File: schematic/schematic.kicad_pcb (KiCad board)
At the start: 2 copper layers, 18 parts, among them U2 74HC595

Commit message: Add outline to pcb
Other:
- board outline added: 66 x 46 mm
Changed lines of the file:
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@@
 		)
+	)
+	(gr_rect
+		(start 92 74.5)
+		(end 158 120.5)
+		(stroke
+			(width 0.1)
+			(type default)
+		)
+		(fill no)
+		(layer "Edge.Cuts")
 	)
 	(segment

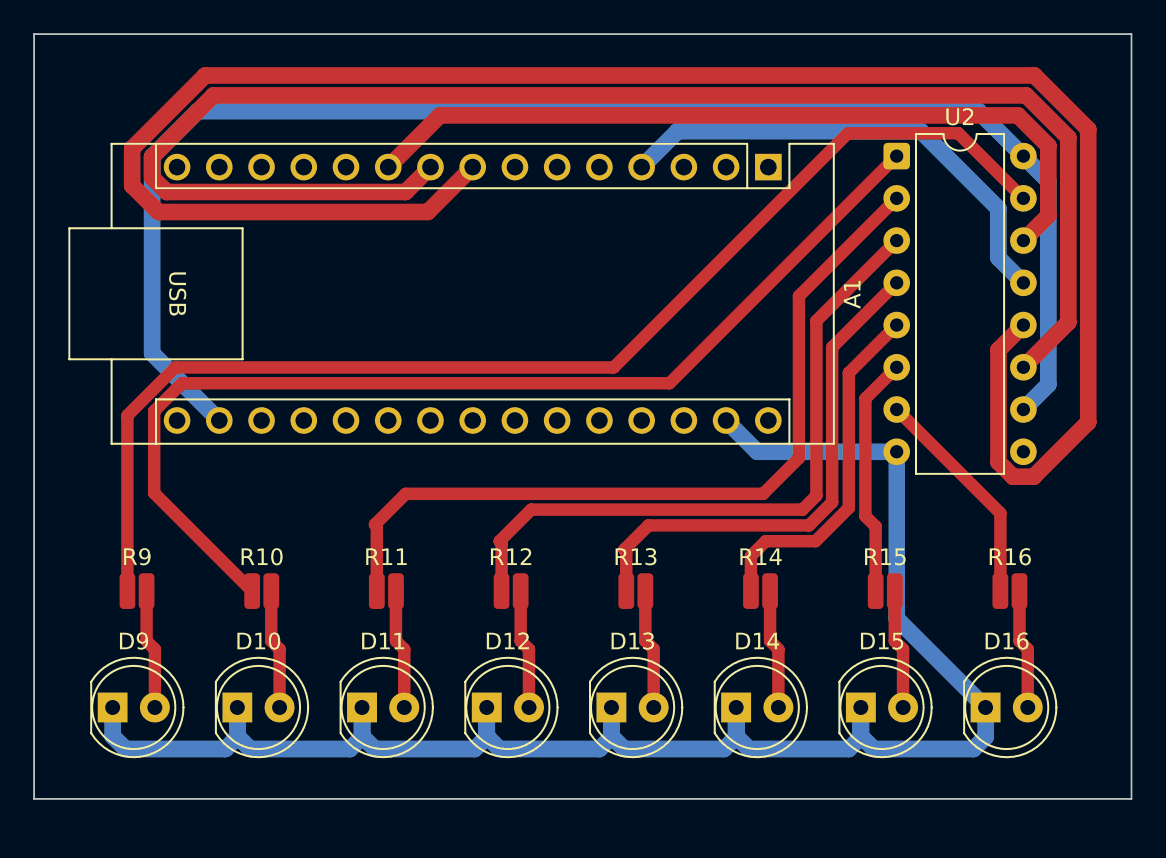
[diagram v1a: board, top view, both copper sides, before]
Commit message: Update schematic to use correct, non-surface mount resistors
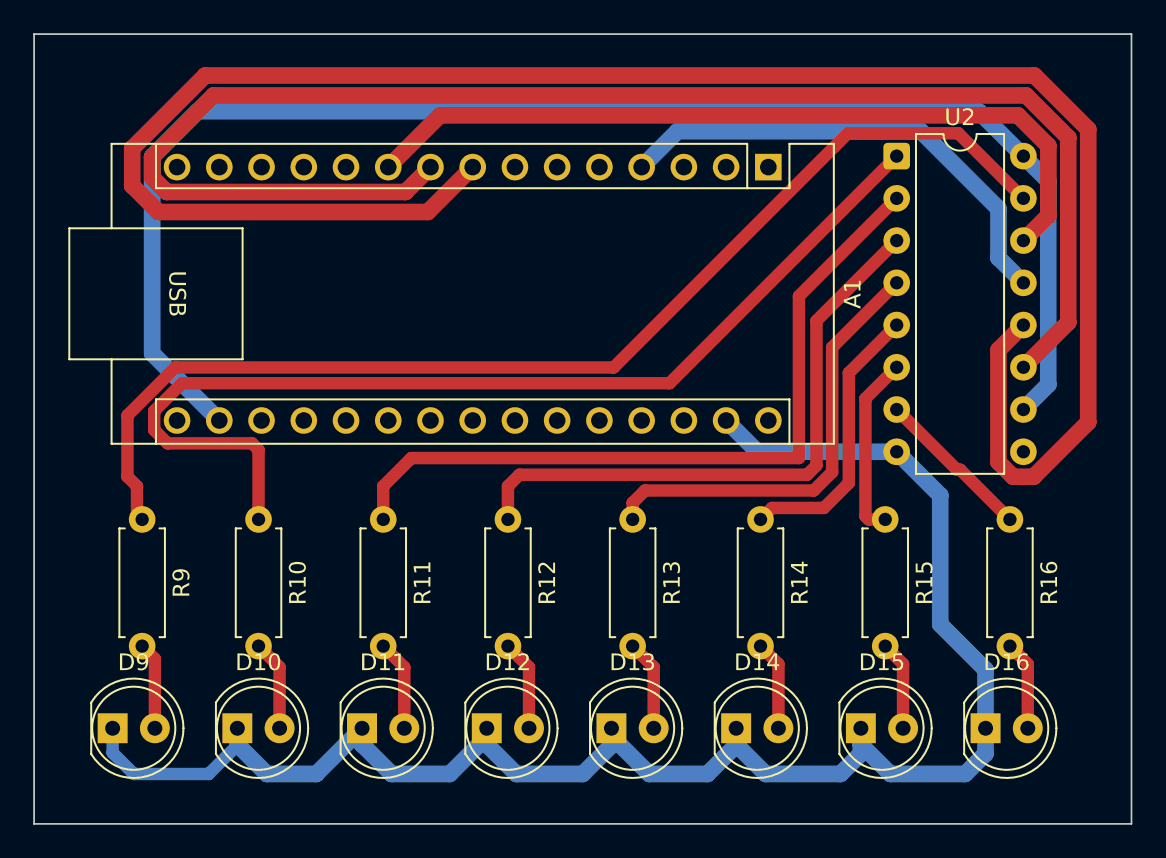
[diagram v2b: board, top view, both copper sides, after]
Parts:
- R10, R11, R12, R13, R14, R15, R16, R9: footprint Resistor_SMD:R_0508_1220Metric -> Resistor_THT:R_Axial_DIN0207_L6.3mm_D2.5mm_P7.62mm_Horizontal
- moved R9 4.32 mm to (98.5, 103.7), turned to -90 degrees
- moved R10 4.31 mm to (105.5, 103.7), turned to -90 degrees
- moved R11 4.31 mm to (113.0, 103.7), turned to -90 degrees
- moved R12 4.31 mm to (120.5, 103.7), turned to -90 degrees
- moved R13 4.31 mm to (128.0, 103.7), turned to -90 degrees
- moved R14 4.31 mm to (135.7, 103.7), turned to -90 degrees
- moved R15 4.31 mm to (143.2, 103.7), turned to -90 degrees
- moved R16 4.31 mm to (150.7, 103.7), turned to -90 degrees
- moved D10 1.25 mm to (104.2, 116.2)
- moved D11 1.25 mm to (111.7, 116.2)
- moved D12 1.25 mm to (119.2, 116.2)
- moved D13 1.25 mm to (126.7, 116.2)
- moved D14 1.25 mm to (134.2, 116.2)
- moved D15 1.25 mm to (141.7, 116.2)
- moved D16 1.25 mm to (149.2, 116.2)
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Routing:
- net Net-(U2-QF): track 21.4 -> 16.9 mm
- net Net-(U2-QE): track 31.0 -> 26.8 mm
- net Net-(U2-QD): track 40.6 -> 36.6 mm
- net Net-(U2-QH): track 13.5 -> 9.55 mm
- net Net-(U2-QA): track 73.1 -> 69.2 mm
- net Net-(D10-K): track 139.3 -> 135.6 mm
- net Net-(U2-QC): track 49.3 -> 45.8 mm
- net Net-(U2-QG): track 14.5 -> 11.0 mm
- net Net-(D9-A): track 7.21 -> 5.26 mm
- net Net-(D16-A): track 7.21 -> 5.39 mm
- net Net-(D15-A): track 7.21 -> 5.39 mm
- net Net-(D14-A): track 7.21 -> 5.39 mm
- net Net-(D13-A): track 7.21 -> 5.46 mm
- net Net-(D12-A): track 7.21 -> 5.46 mm
- net Net-(D11-A): track 7.21 -> 5.46 mm
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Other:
- board size 66 x 46 mm -> 66 x 47.5 mm
